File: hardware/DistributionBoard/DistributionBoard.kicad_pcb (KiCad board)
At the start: 2 copper layers, 35 x 25 mm, 4 parts, among them J101 OUT1, J102 OUT2, J103 IN

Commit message: 4層にしてみた
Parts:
- added G***: LOGO, Library:wasa_10mm, F.Cu at (154.9, 74.7)
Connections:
- REF** pad GND: GND -> (no net)
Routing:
- net GND: vias 0 -> 21
- net /+: vias 0 -> 20
- added copper zone on In1.Cu, net /+
- added copper zone on In2.Cu, net GND
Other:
- copper layers 2 -> 4
- board text added: "DistributionBoard v1.0"

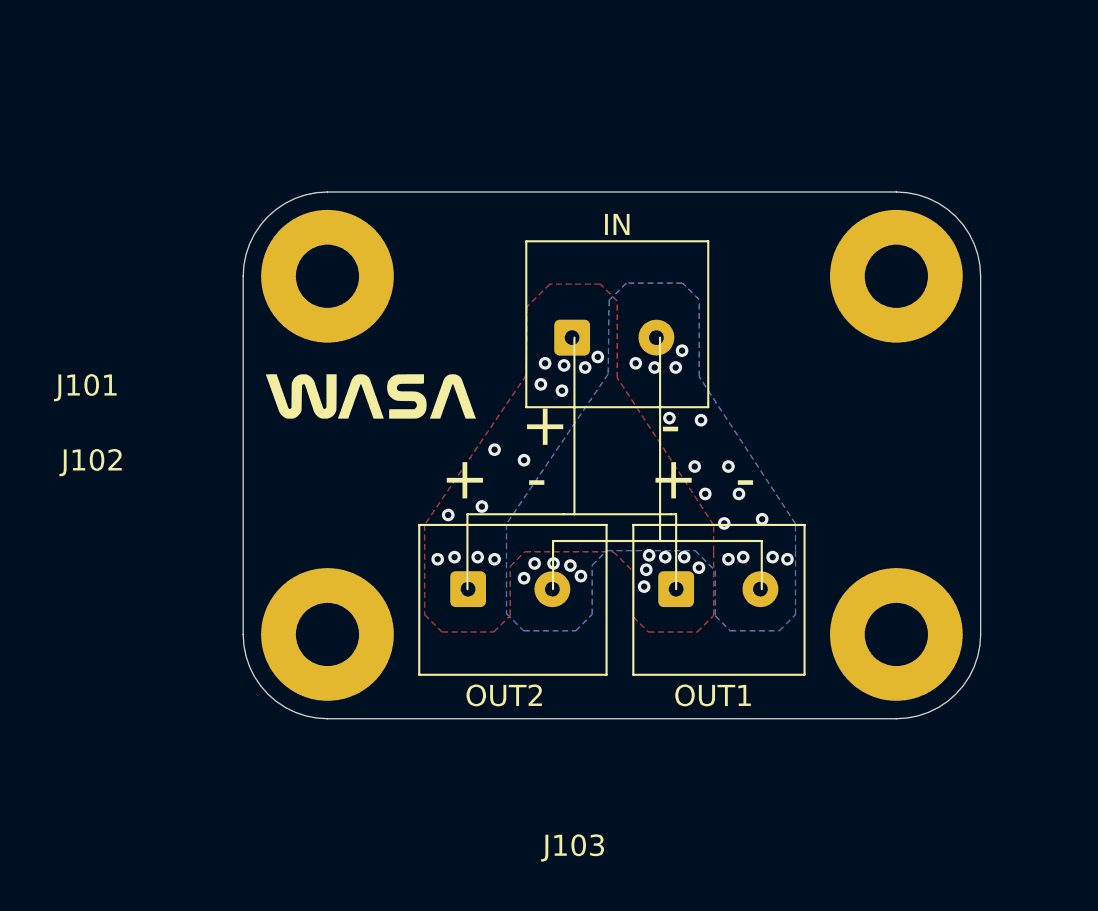
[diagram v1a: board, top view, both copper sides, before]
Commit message: 表面と裏面に分割
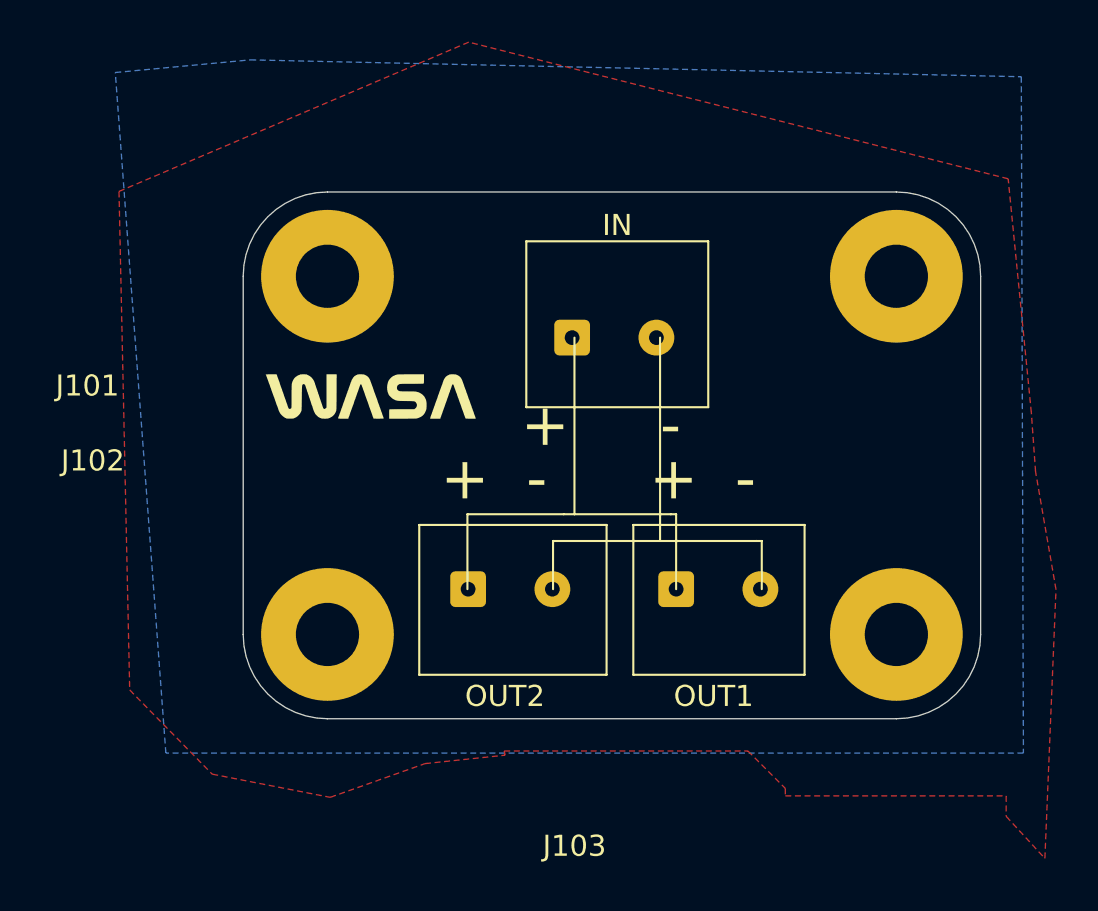
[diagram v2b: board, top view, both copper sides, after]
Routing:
- net GND: vias 21 -> 0
- net /+: vias 20 -> 0
- removed copper zone on In1.Cu, net /+
- removed copper zone on In2.Cu, net GND
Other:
- copper layers 4 -> 2
